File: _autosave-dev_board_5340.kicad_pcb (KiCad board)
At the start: 2 copper layers, 4 parts, among them J5 Conn_01x21_Male, U1 nrf5340, U2 USBLC6-2SC6, U3 W25Q128JVS

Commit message: Refactoring. Start trace
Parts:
- added AE1: Antenna, RF_Antenna:Texas_SWRA117D_2.4GHz_Left, F.Cu at (88.9, 61.6)
- added AE2: Antenna, Connector_Coaxial:U.FL_Hirose_U.FL-R-SMT-1_Vertical, F.Cu at (84.5, 66.0)
- added C1: N.C., Capacitor_SMD:C_0805_2012Metric, F.Cu at (86.7, 69.8)
- added C10: 1uF, Capacitor_SMD:C_0402_1005Metric, F.Cu at (161.7, 78.2)
- added C11: 1uF, Capacitor_SMD:C_0402_1005Metric, F.Cu at (158.9, 78.2)
- added C12: 1uF, Capacitor_SMD:C_0402_1005Metric, F.Cu at (156.0, 78.2)
- added C13: 1uF, Capacitor_SMD:C_0402_1005Metric, F.Cu at (153.1, 78.2)
- added C14: 5uF, Capacitor_SMD:C_0805_2012Metric, F.Cu at (153.9, 75.3)
- added C15: 1uF, Capacitor_SMD:C_0805_2012Metric, F.Cu at (158.4, 71.8)
- added C16: 4.7uF, Capacitor_SMD:C_0805_2012Metric, F.Cu at (162.8, 66.8)
- added C17: 100nF, Capacitor_SMD:C_0402_1005Metric, F.Cu at (166.2, 76.2)
- added C18: 10uF, Capacitor_SMD:C_0805_2012Metric, F.Cu at (149.5, 78.3)
- added C19: C_Small, Capacitor_SMD:C_0805_2012Metric, F.Cu at (86.4, 92.4)
- added C2: 10pF, Capacitor_SMD:C_0805_2012Metric, F.Cu at (91.1, 74.9)
- added C20: C_Small, Capacitor_SMD:C_0805_2012Metric, F.Cu at (88.9, 92.4)
- added C21: 100pF, Capacitor_SMD:C_0805_2012Metric, F.Cu at (171.7, 68.2)
- added C22: 100pF, Capacitor_SMD:C_0805_2012Metric, F.Cu at (176.2, 68.2)
- added C23: 100pF, Capacitor_SMD:C_0805_2012Metric, F.Cu at (162.8, 71.2)
- added C24: 100pF, Capacitor_SMD:C_0805_2012Metric, F.Cu at (145.0, 75.3)
- added C25: 10uF, Capacitor_SMD:C_1206_3216Metric, F.Cu at (162.9, 56.0)
- added C26: 10uF, Capacitor_SMD:C_1206_3216Metric, F.Cu at (168.5, 53.7)
- added C27: 1uF, Capacitor_SMD:C_0805_2012Metric, F.Cu at (149.5, 81.3)
- added C28: 1uF, Capacitor_SMD:C_0402_1005Metric, F.Cu at (76.8, 80.0)
- added C29: 2.2nF, Capacitor_SMD:C_0402_1005Metric, F.Cu at (76.8, 81.3)
- added C3: 10pF, Capacitor_SMD:C_0805_2012Metric, F.Cu at (81.9, 73.0)
- added C4: C_Small, Capacitor_SMD:C_0805_2012Metric, F.Cu at (78.1, 76.2)
- added C5: 1uF, Capacitor_SMD:C_0402_1005Metric, F.Cu at (167.8, 74.2)
- added C6: 1uF, Capacitor_SMD:C_0402_1005Metric, F.Cu at (153.1, 80.1)
- added C7: 1uF, Capacitor_SMD:C_0805_2012Metric, F.Cu at (145.0, 78.3)
- added C8: 1uF, Capacitor_SMD:C_0402_1005Metric, F.Cu at (163.3, 76.2)
- added C9: 1uF, Capacitor_SMD:C_0402_1005Metric, F.Cu at (164.6, 78.2)
- added D1: ASMT-YTC2-0AA02, LED_SMD:LED_Avago_PLCC6_3x2.8mm, F.Cu at (91.6, 70.9)
- added D2: LED, Diode_SMD:D_0603_1608Metric, F.Cu at (176.2, 62.1)
- added D3: LED, Diode_SMD:D_0603_1608Metric, F.Cu at (98.9, 90.2)
- added D4: LED, Diode_SMD:D_0603_1608Metric, F.Cu at (176.2, 59.1)
- added D5: LED, Diode_SMD:D_0603_1608Metric, F.Cu at (171.7, 60.2)
- added D6: LED, Diode_SMD:D_0603_1608Metric, F.Cu at (167.3, 66.8)
- added D7: LED, Diode_SMD:D_0603_1608Metric, F.Cu at (176.2, 65.1)
- added F1: Fuse, Fuse:Fuse_1206_3216Metric, F.Cu at (162.8, 63.6)
- added J1: Conn_01x04_Male, Connector_PinHeader_2.54mm:PinHeader_1x04_P2.54mm_Vertical, F.Cu at (161.8, 44.4)
- added J2: USB_C_Receptacle_USB2.0, Connector_USB:USB_C_Receptacle_XKB_U262-16XN-4BVC11, F.Cu at (81.3, 110.5)
- added J3: Conn_01x02_Male, Connector_PinHeader_2.54mm:PinHeader_1x02_P2.54mm_Vertical, F.Cu at (117.0, 45.8)
- added J4: Conn_01x23, Connector_PinHeader_2.54mm:PinHeader_1x23_P2.54mm_Vertical, F.Cu at (73.7, 57.1)
- added L1: 2.2nH, Inductor_SMD:L_1206_3216Metric, F.Cu at (87.6, 73.7)
- added L2: 10uH, Inductor_SMD:L_1206_3216Metric, F.Cu at (80.3, 80.6)
- added L3: 10uH, Inductor_SMD:L_1206_3216Metric, F.Cu at (80.3, 83.8)
- added R1: 3k5, Resistor_SMD:R_0603_1608Metric, F.Cu at (96.1, 73.0)
- added R10: 0R0, Resistor_SMD:R_0402_1005Metric, F.Cu at (157.7, 56.1)
- added R11: 0R0, Resistor_SMD:R_0402_1005Metric, F.Cu at (165.0, 74.2)
- added R12: 2R2, Resistor_SMD:R_1206_3216Metric, F.Cu at (80.5, 87.0)
- added R13: 2k, Resistor_SMD:R_0402_1005Metric, F.Cu at (89.7, 102.9)
- added R14: 10R, Resistor_SMD:R_1206_3216Metric, F.Cu at (86.4, 99.5)
- added R15: 10R, Resistor_SMD:R_1206_3216Metric, F.Cu at (95.2, 95.2)
- added R16: 1k5, Resistor_SMD:R_0402_1005Metric, F.Cu at (88.9, 98.4)
- added R17: 3k5, Resistor_SMD:R_0603_1608Metric, F.Cu at (148.7, 50.1)
- added R18: 3k5, Resistor_SMD:R_0603_1608Metric, F.Cu at (166.5, 72.2)
- added R19: 3k5, Resistor_SMD:R_0603_1608Metric, F.Cu at (152.4, 63.4)
- added R2: 3k5, Resistor_SMD:R_0603_1608Metric, F.Cu at (96.1, 71.1)
- added R3: 3k.5, Resistor_SMD:R_0603_1608Metric, F.Cu at (96.1, 69.2)
- added R4: R_Small, Resistor_SMD:R_0805_2012Metric, F.Cu at (167.2, 69.8)
- added R5: R_Small, Resistor_SMD:R_0805_2012Metric, F.Cu at (173.5, 53.5)
- added R6: R_Small, Resistor_SMD:R_0603_1608Metric, F.Cu at (148.7, 52.1)
- added R7: 3k, Resistor_SMD:R_0603_1608Metric, F.Cu at (98.9, 92.1)
- added R8: 3k5, Resistor_SMD:R_0603_1608Metric, F.Cu at (144.2, 56.2)
- added R9: 2k0, Resistor_SMD:R_0402_1005Metric, F.Cu at (157.0, 50.1)
- added SW1: SW_Push_Dual_x2, Button_Switch_SMD:SW_Push_1P1T_NO_CK_KSC6xxJ, F.Cu at (98.4, 108.6)
- added SW2: SW_Push_Dual_x2, Button_Switch_SMD:SW_Push_1P1T_NO_CK_KSC6xxJ, F.Cu at (90.8, 108.6)
- added U4: AZ1117-3.3, Package_TO_SOT_SMD:SOT-223, F.Cu at (97.2, 59.3)
- added Y1: Crystal_GND24_Small, Crystal:Crystal_SMD_3225-4Pin_3.2x2.5mm, F.Cu at (81.9, 76.2)
- added Y2: Crystal_Small, Crystal:Crystal_SMD_3215-2Pin_3.2x1.5mm, F.Cu at (87.6, 88.9)
- J5: value Conn_01x21_Male -> Conn_01x23; footprint Connector_PinHeader_2.54mm:PinHeader_1x21_P2.54mm_Vertical -> Connector_PinHeader_2.54mm:PinHeader_1x23_P2.54mm_Vertical
- moved J5 69.6 mm to (104.1, 57.1)
- moved U2 35.6 mm to (81.9, 102.2), turned to 90 degrees
- moved U1 28.8 mm to (87.6, 81.9), turned to 90 degrees
- moved U3 16.6 mm to (95.9, 83.2), turned to 90 degrees
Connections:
- J5 pad 1: (no net) -> /P0.31
- J5 pad 10: (no net) -> /B_LED
- J5 pad 11: (no net) -> /G_LED
- J5 pad 12: (no net) -> /R_LED
- J5 pad 13: (no net) -> /P0.12
- J5 pad 14: (no net) -> /P0.11
- J5 pad 15: (no net) -> /P0.10
- J5 pad 16: (no net) -> /P0.9
- J5 pad 17: (no net) -> /P0.8
- J5 pad 18: (no net) -> /P0.7
- J5 pad 19: (no net) -> /P0.6
- J5 pad 2: (no net) -> /P0.30
- J5 pad 20: (no net) -> /P0.5
- J5 pad 21: (no net) -> /P0.4
- J5 pad 3: (no net) -> /P0.29
- J5 pad 4: (no net) -> /P0.28
- J5 pad 5: (no net) -> /P0.27
- J5 pad 6: (no net) -> /P0.26
- J5 pad 7: (no net) -> /P0.25
- J5 pad 8: (no net) -> /P0.24
- J5 pad 9: (no net) -> /P0.23
- U1 pad A13: (no net) -> Net-(C18-Pad1)
- U1 pad A15: (no net) -> Net-(C15-Pad1)
- U1 pad A17: (no net) -> /P1.13
- U1 pad A21: (no net) -> Net-(L2-Pad2)
- U1 pad A23: (no net) -> Net-(C17-Pad1)
- U1 pad A5: (no net) -> Net-(R12-Pad1)
- U1 pad AA1: (no net) -> Net-(C22-Pad1)
- U1 pad AA31: (no net) -> Net-(J1-Pad3)
- U1 pad AB2: (no net) -> /P0.6
- U1 pad AD2: (no net) -> /P0.7
- U1 pad AE1: (no net) -> /P1.2
- U1 pad AE31: (no net) -> /P0.28
- U1 pad AF2: (no net) -> /P1.3
- U1 pad AH2: (no net) -> /P0.8
- U1 pad AJ1: (no net) -> /P0.9
- U1 pad AK16: (no net) -> /R_LED
- U1 pad AK18: (no net) -> /B_LED
- U1 pad AK2: (no net) -> /P0.10
- U1 pad AK20: (no net) -> /P0.23
- U1 pad AK22: (no net) -> /P1.5
- U1 pad AK24: (no net) -> /P1.7
- U1 pad AK26: (no net) -> /P1.9
- U1 pad AK28: (no net) -> /P0.25
- U1 pad AK30: (no net) -> /P0.27
- U1 pad AK4: (no net) -> /P0.11
- U1 pad AK6: (no net) -> /P0.12
- U1 pad AL15: (no net) -> /G_LED
- U1 pad AL19: (no net) -> /P1.4
- U1 pad AL21: (no net) -> /P1.6
- U1 pad AL23: (no net) -> VDD
- U1 pad AL27: (no net) -> /P0.24
- U1 pad AL29: (no net) -> /P0.26
- U1 pad B10: (no net) -> Net-(L3-Pad2)
- U1 pad B14: (no net) -> /P1.15
- U1 pad B16: (no net) -> /P1.14
- U1 pad B18: (no net) -> /P1.12
- U1 pad B20: (no net) -> /P1.11
- U1 pad B22: (no net) -> /P0.31
- U1 pad B24: (no net) -> /P0.30
- U1 pad B30: (no net) -> Net-(C4-Pad1)
- U1 pad B6: (no net) -> Net-(C16-Pad1)
- U1 pad C31: (no net) -> Net-(C3-Pad1)
- U1 pad L31: (no net) -> Net-(C2-Pad1)
- U1 pad M2: (no net) -> /P1.0
- U1 pad N1: (no net) -> Net-(C19-Pad1)
- U1 pad P2: (no net) -> /P1.1
- U1 pad R1: (no net) -> Net-(C20-Pad1)
- U1 pad R31: (no net) -> /P1.10
- U1 pad U31: (no net) -> /P0.29
- U1 pad V2: (no net) -> /P0.4
- U1 pad VSS: (no net) -> GNDREF
- U1 pad W1: (no net) -> Net-(C21-Pad2)
- U1 pad W31: (no net) -> Net-(J1-Pad2)
- U1 pad Y2: (no net) -> /P0.5
- U2 pad 1: (no net) -> Net-(J2-PadA7)
- U2 pad 3: (no net) -> Net-(J2-PadA6)
- U2 pad 4: (no net) -> Net-(R14-Pad2)
- U2 pad 5: (no net) -> VBUS
- U2 pad 6: (no net) -> Net-(R15-Pad2)

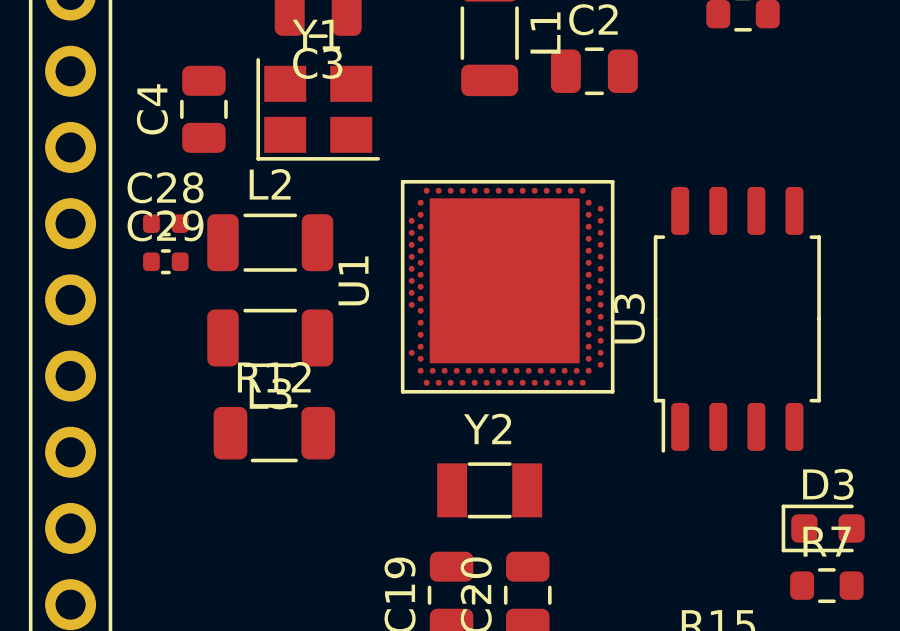
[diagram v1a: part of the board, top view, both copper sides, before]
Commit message: Delete test usb net
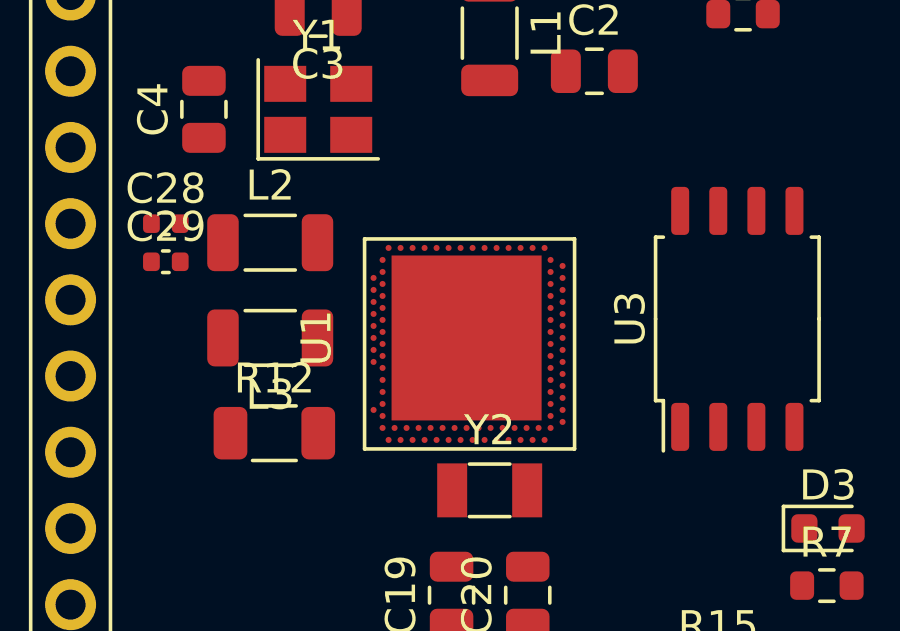
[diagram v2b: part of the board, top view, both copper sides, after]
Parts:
- moved U1 2.29 mm to (86.4, 83.8)
